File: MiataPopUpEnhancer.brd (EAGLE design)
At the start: 100 x 80 mm, 84 parts, among them J3 USB4110-GF-A, Q1 MICRO_COMMERCIAL_MMSS8050-L-T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, Q11 MICRO_COMMERCIAL_MMSS8050-L-T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, Q12 MICRO_COMMERCIAL_MMSS8050-L-T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, Q13 DIODES_INC_DMP3099L-13DIODES_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, Q2 MICRO_COMMERCIAL_MMSS8050-L-T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, Q21 MICRO_COMMERCIAL_MMSS8050-L-T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, Q22 MICRO_COMMERCIAL_MMSS8050-L-T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, Q23 DIODES_INC_DMP3099L-13DIODES_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, Q3 DIODES_INC_DMP3099L-13DIODES_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, Q31 MICRO_COMMERCIAL_MMSS8050-L-T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, Q32 MICRO_COMMERCIAL_MMSS8050-L-T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, Q33 DIODES_INC_DMP3099L-13DIODES_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, SW1 KMR2, U1 ATSAMD21E18A-MUT, U2 MCP1703CB, U3 MDBT40, Y1 ABS25-32.768KHZ-T

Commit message: Continues routing and cleanup of south end of board
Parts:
- Q13, Q23, Q3, Q33: value DIODES_INC_DMP3099L-13DIODES_INC_DMP3099L-13_0_2 -> DIODES_INC_DMP3099L-13DIODES_INC_DMP3099L-13_0_0; device Diodes Inc. - DMP3099L-13:DIODES_INC_DMP3099L-13_2 -> Diodes Inc. - DMP3099L-13:DIODES_INC_DMP3099L-13_0
- moved C21 29.3 mm to (10.8, 14.0)
- moved C31 29.3 mm to (17.8, 14.0)
- moved D21 29.3 mm to (8.26, 9.53)
- moved D31 29.3 mm to (15.2, 9.53)
- moved D33 29.3 mm to (14.6, 14.6)
- moved Q31 29.3 mm to (14.6, 18.1)
- moved R21 29.3 mm to (10.8, 12.1)
- moved R23 29.3 mm to (10.8, 17.8)
- moved R31 29.3 mm to (17.8, 12.1)
- moved R32 29.3 mm to (14.6, 12.1)
- moved R33 29.3 mm to (17.8, 17.8)
- moved S21 29.3 mm to (10.8, 15.9)
- moved S31 29.3 mm to (17.8, 15.9)
- moved D2 29.3 mm to (11.1, 7.94)
- moved D23 29.3 mm to (7.62, 14.6)
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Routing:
- net +12V: track 17.5 -> 84.2 mm, vias 0 -> 6
- net DASH_IND_RH: track 1.95 -> 41.2 mm
- net DASH_IND_LH_12V: track 0.00 -> 25.1 mm, vias 0 -> 3
- net DASH_IND_RH_12V: track 0.00 -> 24.6 mm, vias 0 -> 3
- net +3V3: track 24.2 -> 48.1 mm, vias 3 -> 5
- net DASH_IND_12V: track 0.00 -> 22.7 mm, vias 0 -> 1
- net DOWN_OUT_LH: track 5.28 -> 23.8 mm, vias 2 -> 1
- net GND: track 17.4 -> 34.1 mm, vias 8 -> 62
- net UP_OUT_LH: track 4.96 -> 18.7 mm, vias 2 -> 1
- net DASH_IND_LH: track 2.12 -> 15.4 mm
- net UP_OUT_RH: track 5.34 -> 17.8 mm, vias 2 -> 1
- net N$13: track 0.00 -> 11.4 mm, vias 0 -> 3
- net N$3: track 0.00 -> 10.8 mm, vias 0 -> 3
- net DASH_IND_RH_FILT: track 0.00 -> 9.69 mm
- net DASH_IND_LH_FILT: track 0.00 -> 9.42 mm
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- added copper zone on layer 1, net GND
- added copper zone on layer 16, net GND

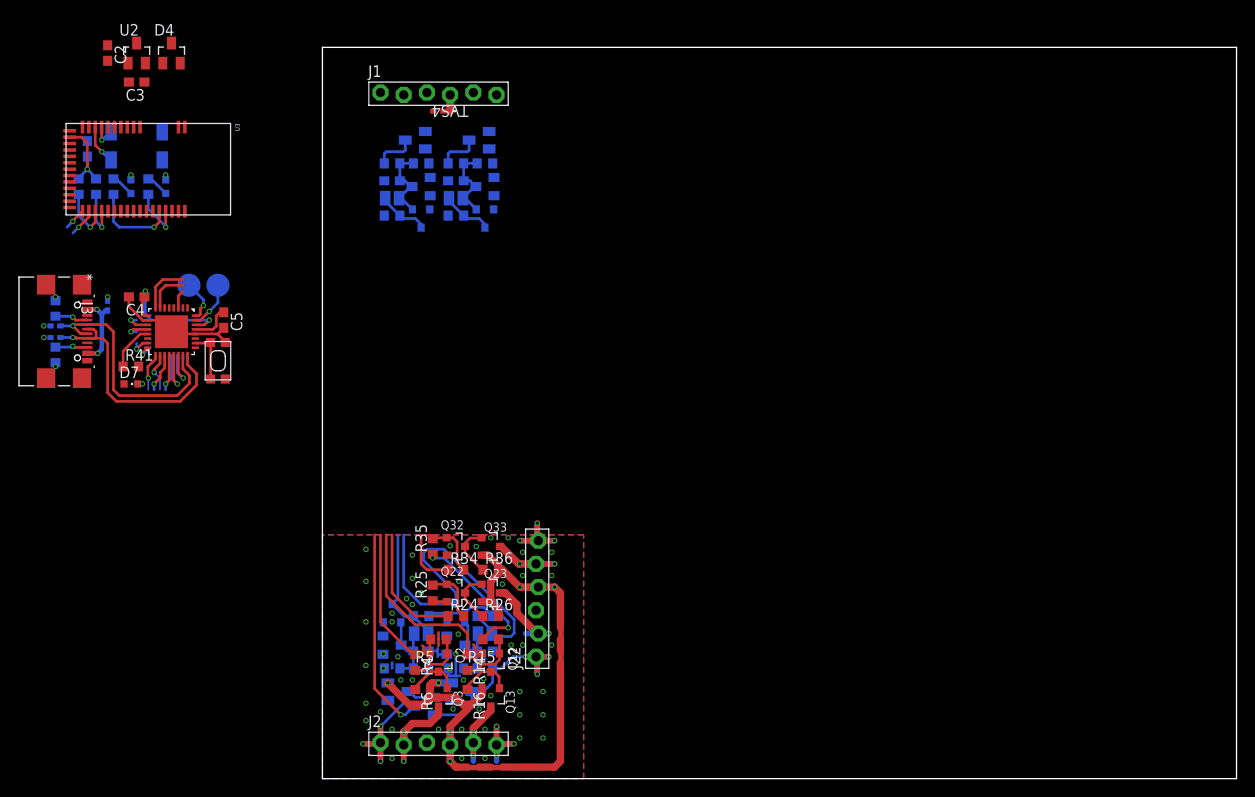
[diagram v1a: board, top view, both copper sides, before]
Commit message: First complete layout. Still using headers for connectors
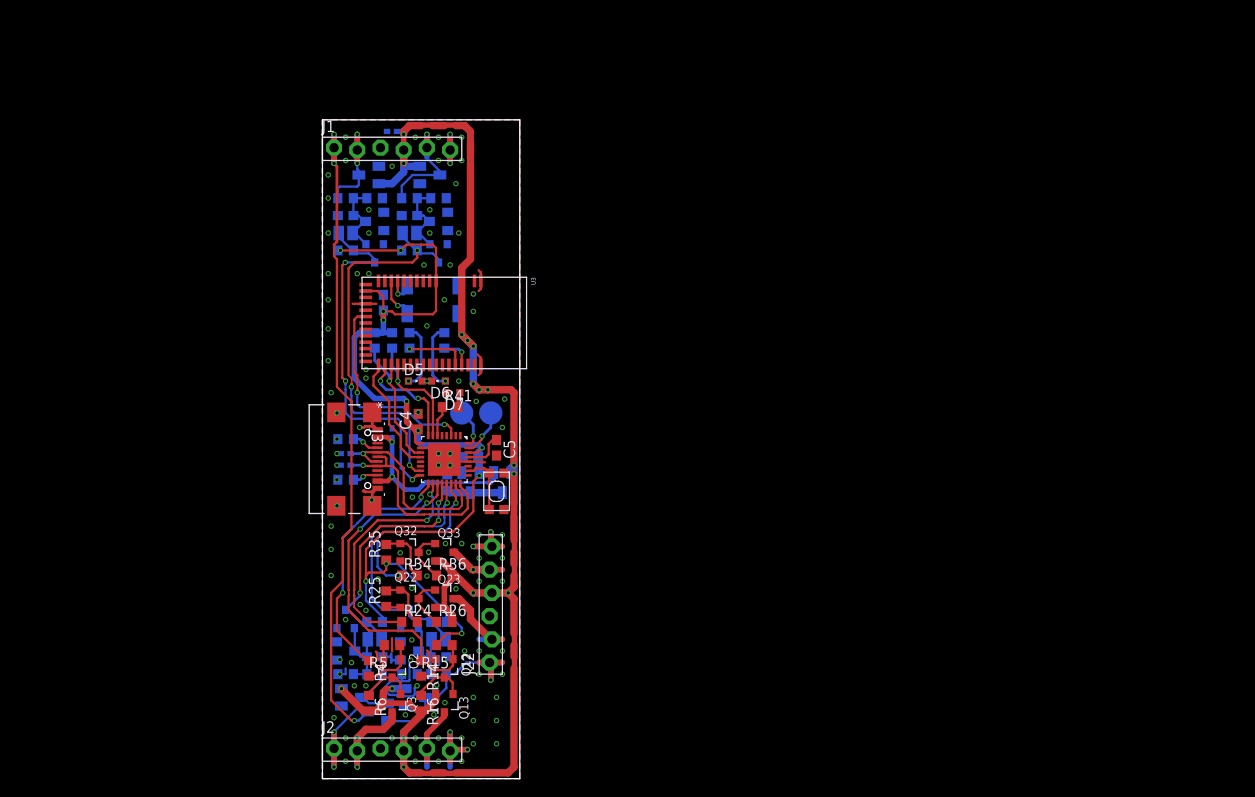
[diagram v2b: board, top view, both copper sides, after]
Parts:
- C2: device adafruit:C0603 -> adafruit:C0603K
- moved C2 59.9 mm to (13.7, 32.4), flipped to the bottom, turned to 90 degrees
- moved U2 59.5 mm to (16.2, 32.4), flipped to the bottom, turned to 180 degrees
- moved D4 59.3 mm to (19.7, 32.4), flipped to the bottom, turned to 180 degrees
- moved C3 54.9 mm to (16.2, 35.2), flipped to the bottom, turned to 0 degrees
- moved D5 37.7 mm to (10.2, 43.5), flipped to the top, turned to 270 degrees
- moved D6 36.7 mm to (12.7, 43.5), flipped to the top, turned to 90 degrees
- moved U3 36.5 mm to (13.3, 49.8)
- moved C6 36.5 mm to (6.67, 52.1)
- moved R42 36.5 mm to (7.62, 47.9)
- moved R43 36.5 mm to (5.71, 47.9)
- moved R44 36.5 mm to (9.53, 47.9)
- moved R45 36.5 mm to (13.3, 47.9)
- moved Y1 36.5 mm to (12.1, 52.4)
- moved D7 35.3 mm to (14.3, 42.2), turned to 90 degrees
- moved R41 35.2 mm to (14.0, 40.6)
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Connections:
- net DASH_IND_LH: now also U1.20; no longer U1.15
- net DASH_IND_RH: now also U1.21; no longer U1.16
- net DEBUG_LED: now also U1.6; no longer U1.13
- net DOWN_OUT_RH: now also U1.22; no longer U1.17
- net DOWN_REQ: now also U1.15; no longer U1.21
- net GND: now also J3.15, J3.16, J3.17, J3.18
- net UP_OUT_LH: now also U1.17; no longer U1.20
- net UP_REQ: now also U1.16; no longer U1.22
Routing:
- net +12V: track 84.2 -> 163.4 mm, vias 6 -> 16
- net +3V3: track 48.1 -> 114.1 mm, vias 5 -> 11
- net DASH_IND_12V: track 22.7 -> 72.4 mm, vias 1 -> 3
- net DOWN_REQ: track 12.4 -> 43.3 mm, vias 1 -> 3
- net UP_REQ: track 11.2 -> 40.1 mm, vias 1 -> 3
- net BLE_MODE: track 2.06 -> 22.9 mm, vias 0 -> 2
- net GND: track 34.1 -> 51.5 mm, vias 62 -> 106
- net VBUS: track 8.20 -> 20.7 mm
- net DASH_IND_LH: track 15.4 -> 27.1 mm, vias 1 -> 3
- net DASH_IND_RH: track 41.2 -> 30.6 mm
- net DOWN_OUT_RH: track 10.5 -> 19.9 mm, vias 1 -> 2
- net UP_OUT_LH: track 18.7 -> 27.7 mm, vias 1 -> 2
- net UP_OUT_RH: track 17.8 -> 26.5 mm, vias 1 -> 2
- net DOWN_OUT_LH: track 23.8 -> 32.3 mm, vias 1 -> 2
- net BLE_RTS: track 5.03 -> 13.1 mm, vias 2 -> 0
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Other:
- board size 100 x 80 mm -> 21.6 x 72.1 mm
